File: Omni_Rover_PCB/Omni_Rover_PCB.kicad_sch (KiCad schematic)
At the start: 6 parts, among them J2 USB_C_Receptacle_USB2.0_16P, U5 USBLC6-2SC6

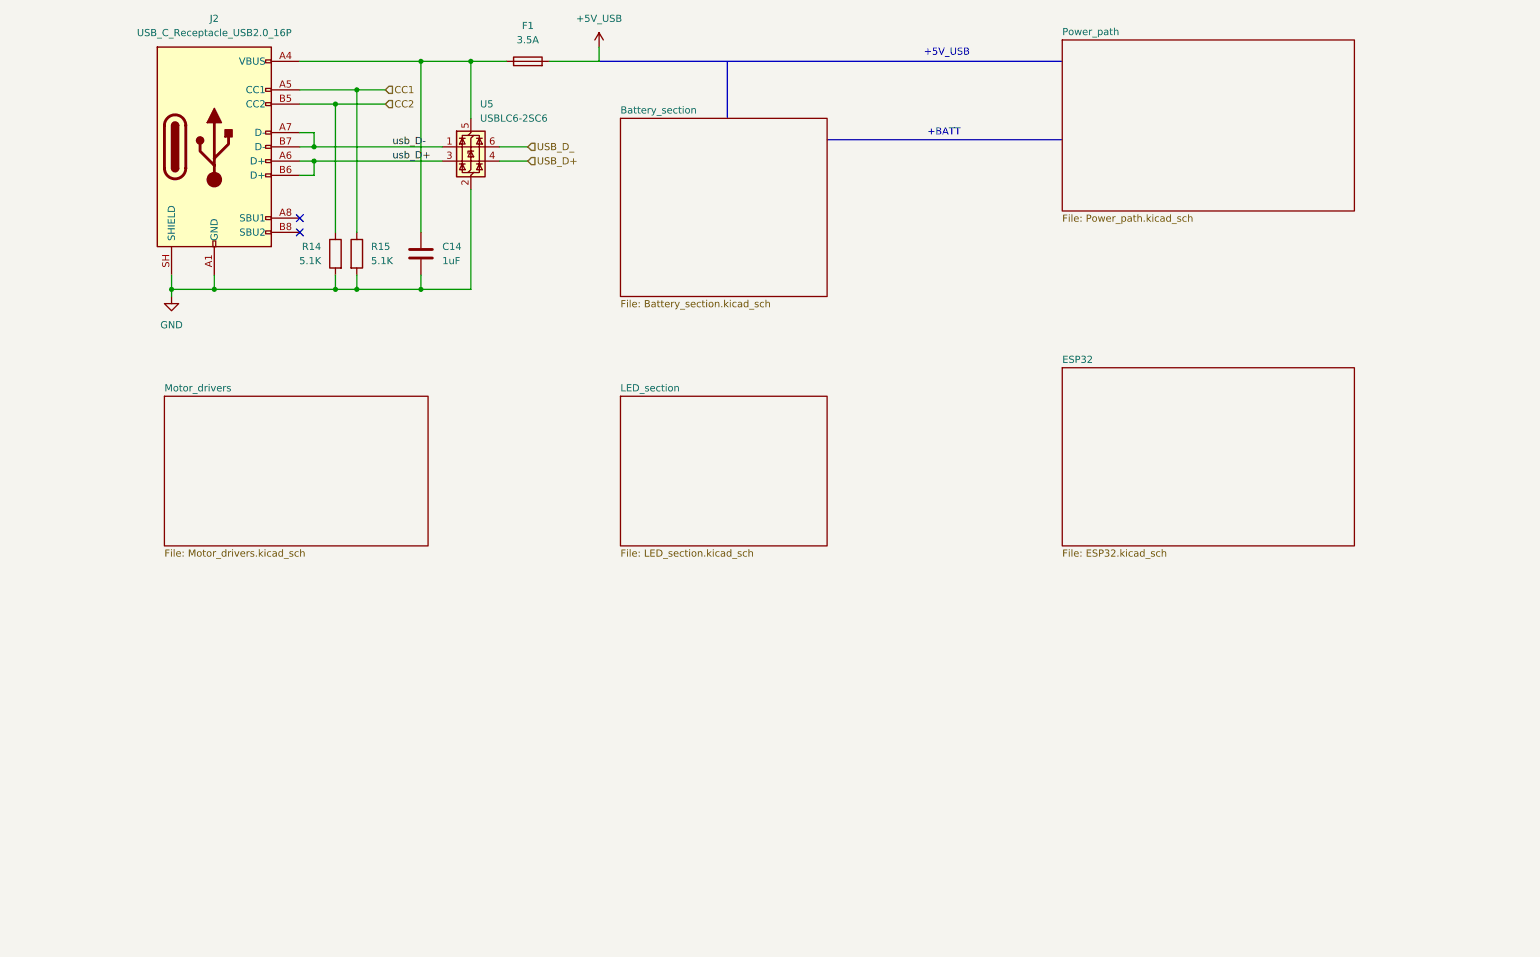
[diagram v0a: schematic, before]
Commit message: Finished the Laout 0 DRC ERRORS. Just needs some finishing touches.
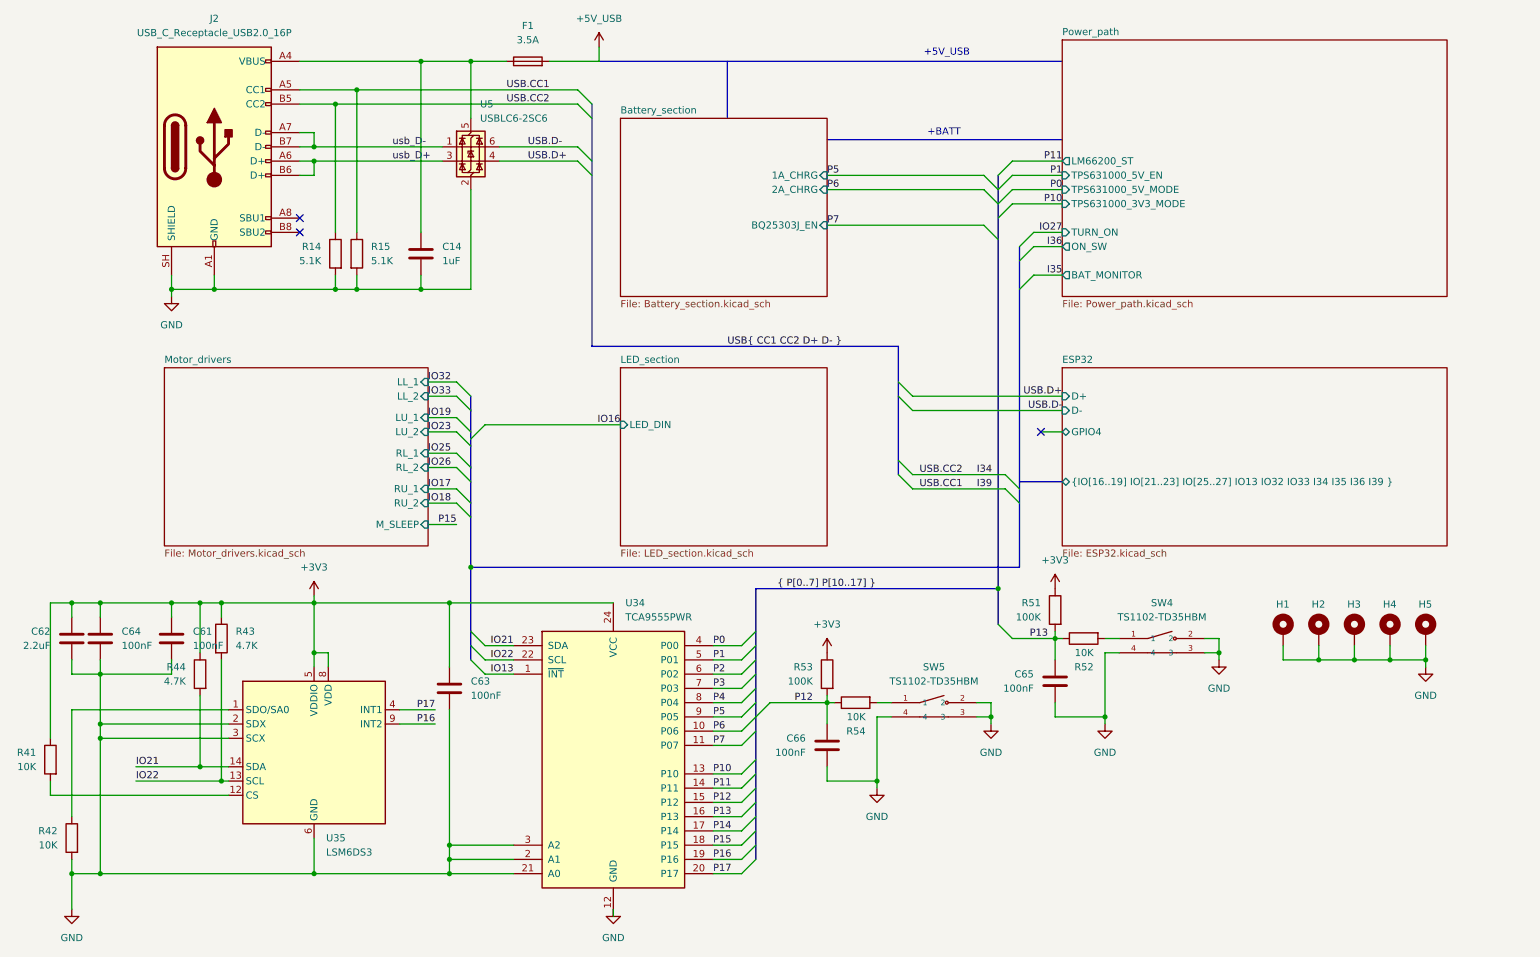
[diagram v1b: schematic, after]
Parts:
- added C61, C63, C64, C65, C66: 100nF, Capacitor_SMD:C_0402_1005Metric_Pad0.74x0.62mm_HandSolder, symbol Device:C
- added C62: 2.2uF, Capacitor_SMD:C_0402_1005Metric_Pad0.74x0.62mm_HandSolder, symbol Device:C
- added H1, H2, H3, H4, H5: MountingHole_Pad, MountingHole:MountingHole_3.2mm_M3_Pad_Via, symbol Mechanical:MountingHole_Pad
- added R41, R42, R52, R54: 10K, Resistor_SMD:R_0402_1005Metric_Pad0.72x0.64mm_HandSolder, symbol Device:R
- added R43, R44: 4.7K, Resistor_SMD:R_0402_1005Metric_Pad0.72x0.64mm_HandSolder, symbol Device:R
- added R51, R53: 100K, Resistor_SMD:R_0402_1005Metric_Pad0.72x0.64mm_HandSolder, symbol Device:R
- added SW4, SW5: TS1102-TD35HBM, lcsc_footprints:C36936640_SW-SMD_TS1102-TD35HBM, symbol lcsc_imported:TS1102-TD35HBM
- added U34: TCA9555PWR, Package_SO:TSSOP-24_4.4x7.8mm_P0.65mm, symbol Interface_Expansion:TCA9555PWR
- added U35: LSM6DS3, Package_LGA:LGA-14_3x2.5mm_P0.5mm_LayoutBorder3x4y, symbol Sensor_Motion:LSM6DS3
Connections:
- net GND: now also C61.1, C62.2, C63.1, C64.1, C65.1, C66.1, H1.1, H2.1, H3.1, H4.1, H5.1, R42.2, SW4.2, SW4.3, SW4.4, SW5.2, SW5.3, SW5.4, U34.12 (GND), U34.2 (A1), U34.21 (A0), U34.3 (A2), U35.2 (SDX), U35.3 (SCX), U35.6 (GND), U35.7 (GND)
- net CC1 renamed I39
- net CC2 renamed I34
- net USB_D+ renamed USB.D+
- net USB_D_ renamed USB.D-
- new net: R52.2, SW4.1
- new net: R54.2, SW5.1
- new net: R42.1, U35.1 (SDO/SA0)
- new net: R41.2, U35.12 (CS)
- new net +3V3: C61.2, C62.1, C63.2, C64.2, R41.1, R43.1, R44.1, R51.1, R53.1, U34.24 (VCC), U35.5 (VDDIO), U35.8 (VDD)
- new net IO13: U34.1 (~{INT})
- new net IO21: R44.2, U34.23 (SDA), U35.14 (SDA)
- new net IO22: R43.2, U34.22 (SCL), U35.13 (SCL)
- new net P0: U34.4 (P00)
- new net P1: U34.5 (P01)
- new net P10: U34.13 (P10)
- new net P11: U34.14 (P11)
- new net P12: C66.2, R53.2, R54.1, U34.15 (P12)
- new net P13: C65.2, R51.2, R52.1, U34.16 (P13)
- new net P14: U34.17 (P14)
- new net P15: U34.18 (P15)
- new net P16: U34.19 (P16), U35.9 (INT2)
- new net P17: U34.20 (P17), U35.4 (INT1)
- new net P2: U34.6 (P02)
- new net P3: U34.7 (P03)
- new net P4: U34.8 (P04)
- new net P5: U34.9 (P05)
- new net P6: U34.10 (P06)
- new net P7: U34.11 (P07)
- no-connect marks 2 -> 3
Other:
- sheet Battery_section ports: added 1A_CHRG, 2A_CHRG, BQ25303J_EN; removed none
- sheet ESP32 ports: added D+, D-, GPIO4, {IO[16..19] IO[21..23] IO[25..27] IO13 IO32 IO33 I34 I35 I36 I39 }; removed none
- sheet LED_section ports: added LED_DIN; removed none
- sheet Motor_drivers ports: added LL_1, LL_2, LU_1, LU_2, M_SLEEP, RL_1, RL_2, RU_1, RU_2; removed none
- sheet Power_path ports: added BAT_MONITOR, LM66200_ST, ON_SW, TPS631000_3V3_MODE, TPS631000_5V_EN, TPS631000_5V_MODE, TURN_ON; removed none

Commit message: Made soem minor fixes to the schematic and PCB layout.
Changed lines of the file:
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@@
 	(bus
 		(pts
-			(xy 173.99 90.17) (xy 173.99 99.06)
+			(xy 173.99 88.9) (xy 173.99 99.06)
 		)
 		(stroke
@@
 	(bus
 		(pts
-			(xy 119.38 90.17) (xy 173.99 90.17)
+			(xy 119.38 88.9) (xy 173.99 88.9)
 		)
 		(stroke
@@
 	(bus
 		(pts
-			(xy 119.38 46.99) (xy 119.38 90.17)
+			(xy 119.38 46.99) (xy 119.38 88.9)
 		)
 		(stroke
@@
 	)
 	(label "USB{ CC1 CC2 D+ D- }"
-		(at 143.51 90.17 0)
-		(effects
-			(font
+		(at 143.51 88.9 0)
+		(effects
+			(font
